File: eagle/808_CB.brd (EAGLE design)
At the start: 100 x 80 mm, 54 parts, among them IC1 4584N, IC4 TL072P, Q1 2N3904, Q2 2N3904, Q3 2N3904, Q8 2N3906

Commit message: starting board part by part
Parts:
- moved R15* 127.8 mm to (-77.5, 62.2), turned to 0 degrees
- moved C7 127.2 mm to (-31.8, 41.9)
- moved R16 109.2 mm to (-16.5, 68.6)
- moved IC4 101.8 mm to (-71.1, 31.8), turned to 0 degrees
- moved R166* 99.6 mm to (-63.5, 49.5), turned to 0 degrees
- moved PWR1 88.4 mm to (-47.0, 33.0)
- moved OUT_NORM 86.8 mm to (-62.2, 31.8), turned to 0 degrees
- moved R22 86.5 mm to (-62.2, 68.6), turned to 0 degrees
- moved C4 76.3 mm to (-55.9, 48.3)
- moved C10 70.0 mm to (-50.8, 41.9), turned to 0 degrees
- moved C9 69.0 mm to (-44.5, 41.9)
- moved R4 68.6 mm to (-54.6, 55.9), turned to 0 degrees
- moved C12 68.1 mm to (-57.1, 41.9), turned to 0 degrees
- moved C3 65.4 mm to (-45.7, 48.3), turned to 0 degrees
- moved C8 63.1 mm to (-38.1, 41.9), turned to 0 degrees
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
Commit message: part by part
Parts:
- removed 540HZ, 800HZ: 200k, pot:3RP/1610N
- removed IC4: TL072P, linear:DIL08
- removed R166*: 1K, TR808clone:0207/5V
- removed R3*: 22K, TR808clone:0207/5V
- added IC2: TL072P, linear:DIL08
- added R26: 1k, TR808clone:0207/5V
- added R27: 8k2, TR808clone:0207/5V
- added R29: 22k, TR808clone:0207/5V
- added R30: 1K, TR808clone:0207/5V
- C10: value 3.3n -> 0.47uF/50; device TR808clone:C035-025X75 -> rcl:B45181A
- C5: value 0.47uF/50 -> 2.2n; device rcl:B45181A -> TR808clone:C035-025X75
- C6: value 1uF/50 -> 2.2n; device rcl:B45181A -> TR808clone:C035-025X75
- C7: value 2.2n -> 3.3n
- C8: value 2.2n -> 10n
- C9: value 10n -> 1uF/50; device TR808clone:C035-025X75 -> rcl:B45181A
- R10, R9: value 470k -> 2k2
- R11, R12: value 100R -> 470k
- R13: value 1k -> 100R
- R14: value 33k -> 100R
- R20: value 470k -> 33k
- R21: value 8k2 -> 470k
- R22: value 22k -> 22K
- R3, R4: value 33k -> 200k; device TR808clone:0207/5V -> pot:3RP/1610N
- R7, R8: value 2k2 -> 33k
- moved R22 114.9 mm to (43.2, 22.9)
- moved R15 101.4 mm to (27.9, 35.6), turned to 180 degrees
- moved C5 97.5 mm to (24.1, 26.7), turned to 270 degrees
- moved D1 96.8 mm to (33.0, 40.6), turned to 90 degrees
- moved R11 95.2 mm to (24.1, 49.5), turned to 270 degrees
- moved D2 93.2 mm to (19.1, 40.6), turned to 90 degrees
- moved C12 92.5 mm to (29.2, 8.89)
- moved R21 86.3 mm to (17.8, 21.6), turned to 180 degrees
- moved R13 82.9 mm to (25.4, 40.6)
- moved R14 78.0 mm to (12.7, 40.6), turned to 180 degrees
- moved C3 75.0 mm to (29.2, 52.1), turned to 90 degrees
- moved R19 71.1 mm to (22.9, 34.3), turned to 270 degrees
- moved C4 70.0 mm to (14.0, 52.1), turned to 90 degrees
- moved R17 65.9 mm to (30.5, 31.8)
- moved R9 63.7 mm to (31.8, 57.1), turned to 180 degrees
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- renumbered 540HZ1 to R28, OUTPUT to JCK1, OUT_NORM to X1, Q8 to Q4, R10* to R25, R15* to R24, R6* to R23
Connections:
- net +15V: now also IC2.8, R11.2, R12.2; no longer IC4.8, R10.2, R9.2
- net -15V: now also IC2.4; no longer IC4.4
- net CY_OUT: now also R30.2; no longer R166*.2
- net GND: now also C10.-, C9.-, IC2.3, R10.1, R13.1, R14.1, R29.1, R9.1; no longer C5.-, C6.-, IC4.3, R11.1, R12.1, R22.1, R7.1, R8.1
- net LT: now also R22.2; no longer R3*.2
- net N$10: now also R9.2; no longer R3.2
- net N$11: now also R12.1; no longer R10.1
- net N$12: now also R11.1; no longer R9.1
- net N$13: now also R13.2; no longer R11.2
- net N$14: now also R14.2; no longer R12.2
- net N$15: now also D2.C; no longer D1.C
- net N$16: now also D1.C; no longer D2.C
- net N$17: now also C10.+, R20.2; no longer C5.+, R14.2
- net N$18: now also R26.2; no longer R13.2
- net N$19: now also R26.1; no longer R13.1
- net N$20: now also C9.+, R20.1; no longer C6.+, R14.1
- net N$21: now also D2.A; no longer D1.A
- net N$22: now also D1.A; no longer D2.A
- net N$23: now also C5.P$1; no longer C8.P$1
- net N$24: now also C6.P$1; no longer C7.P$1
- net N$25: now also C5.P$2, C6.P$2, C7.P$1, C8.P$1; no longer C10.P$1, C7.P$2, C8.P$2, C9.P$1
- net N$26: now also C8.P$2, IC2.2, R21.1; no longer C9.P$2, IC4.2, R20.1
- net N$27: now also C7.P$2, IC2.1, R21.2; no longer C10.P$2, IC4.1, R20.2
- net N$29: now also R27.1; no longer R21.1
- net N$30: now also R27.2; no longer R21.2
- net N$32: now also IC2.5, R29.2; no longer IC4.5, R22.2
- net N$33: now also IC2.6, IC2.7, R30.1; no longer IC4.6, IC4.7, R166*.1
- net N$4: now also R4.2; no longer 800HZ.2
- net N$5: now also R3.2; no longer 540HZ.2
- net N$517: now also R22.1; no longer R3*.1
- net N$6: now also R7.1; no longer R3.1
- net N$7: now also R3.3; no longer 540HZ.3
- net N$8: now also R4.3; no longer 800HZ.3
- net N$9: now also R10.2; no longer R4.2
- net TP7: now also R8.1; no longer R4.1

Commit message: parts on the board
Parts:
- moved R23 123.2 mm to (45.7, 54.6), turned to 270 degrees
- moved C10 121.3 mm to (47.0, 62.2), turned to 270 degrees
- moved Q4 120.3 mm to (41.9, 44.5)
- moved R24 116.9 mm to (38.1, 44.5), turned to 270 degrees
- moved R20 106.8 mm to (44.5, 67.3)
- moved R26 98.6 mm to (43.2, 49.5), turned to 180 degrees
- moved Q3 94.4 mm to (41.9, 55.9), turned to 180 degrees
- moved PWR1 92.9 mm to (44.5, 16.5), turned to 90 degrees
- moved X1 88.0 mm to (21.6, 5.08), turned to 90 degrees
- moved R25 85.4 mm to (38.1, 54.6), turned to 270 degrees
- moved D3 73.6 mm to (44.5, 39.4), turned to 180 degrees
- moved C9 66.3 mm to (41.9, 62.2), turned to 270 degrees
- moved R22 21.7 mm to (45.7, 44.5), turned to 270 degrees
- moved R29 6.84 mm to (29.2, 8.89), turned to 0 degrees
- moved R30 4.02 mm to (21.6, 12.7)
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- renumbered R28 to LEVEL, R3 to TUNE_1, R4 to TUNE_2

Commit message: routed
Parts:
- R8: device TR808clone:0207/5V -> TR808clone:0207/7
- moved R26 12.5 mm to (41.9, 37.1), turned to 0 degrees
- moved D3 10.5 mm to (36.1, 33.0), turned to 90 degrees
- moved R30 9.44 mm to (18.4, 3.81)
- moved R16 7.13 mm to (24.9, 34.8)
- moved R5 6.12 mm to (13.7, 66.8), turned to 0 degrees
- moved C12 5.99 mm to (26.0, 10.2)
- moved R13 4.33 mm to (25.1, 45.0)
- moved D2 3.94 mm to (15.2, 39.6)
- moved R29 3.59 mm to (31.8, 6.35)
- moved R15 3.59 mm to (30.5, 38.1), turned to 90 degrees
- moved C11 3.34 mm to (21.1, 17.0), turned to 90 degrees
- moved R19 3.31 mm to (19.6, 34.5)
- moved R23 3.09 mm to (48.8, 54.1)
- moved C5 2.97 mm to (26.9, 25.7), turned to 180 degrees
- moved R18 2.84 mm to (14.0, 31.8), turned to 0 degrees
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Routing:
- net GND: track 0.00 -> 268.4 mm
- net +5V: track 0.00 -> 101.6 mm
- net +15V: track 0.00 -> 77.6 mm
- net N$7: track 0.00 -> 52.6 mm, vias 0 -> 2
- net N$17: track 0.00 -> 49.8 mm
- net N$33: track 0.00 -> 34.9 mm
- net -15V: track 0.00 -> 33.7 mm
- net N$5: track 0.00 -> 31.1 mm
- net N$31: track 0.00 -> 26.9 mm
- net N$27: track 0.00 -> 26.4 mm
- net TRIG*: track 0.00 -> 23.9 mm
- net N$25: track 0.00 -> 21.2 mm
- net N$8: track 0.00 -> 17.1 mm
- net LT: track 0.00 -> 15.9 mm
- net N$32: track 0.00 -> 14.9 mm
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
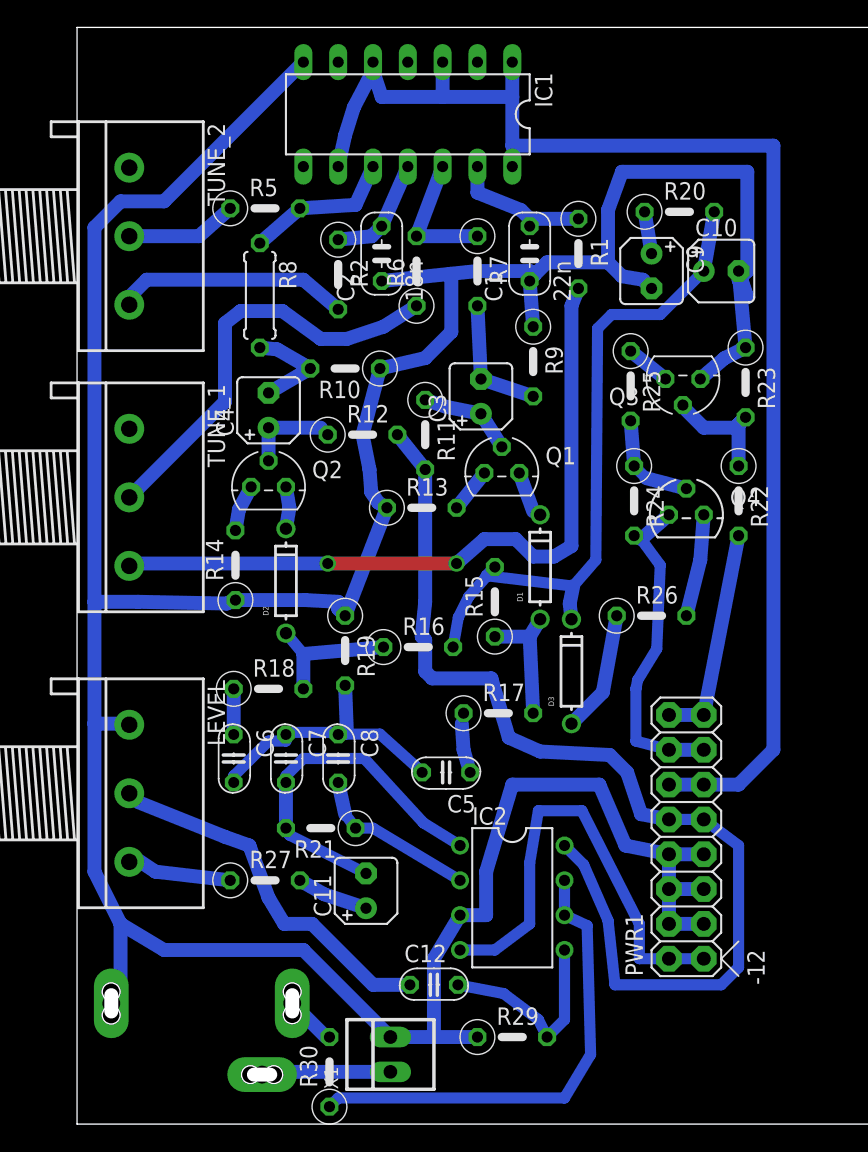
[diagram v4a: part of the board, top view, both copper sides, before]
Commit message: thicker traces
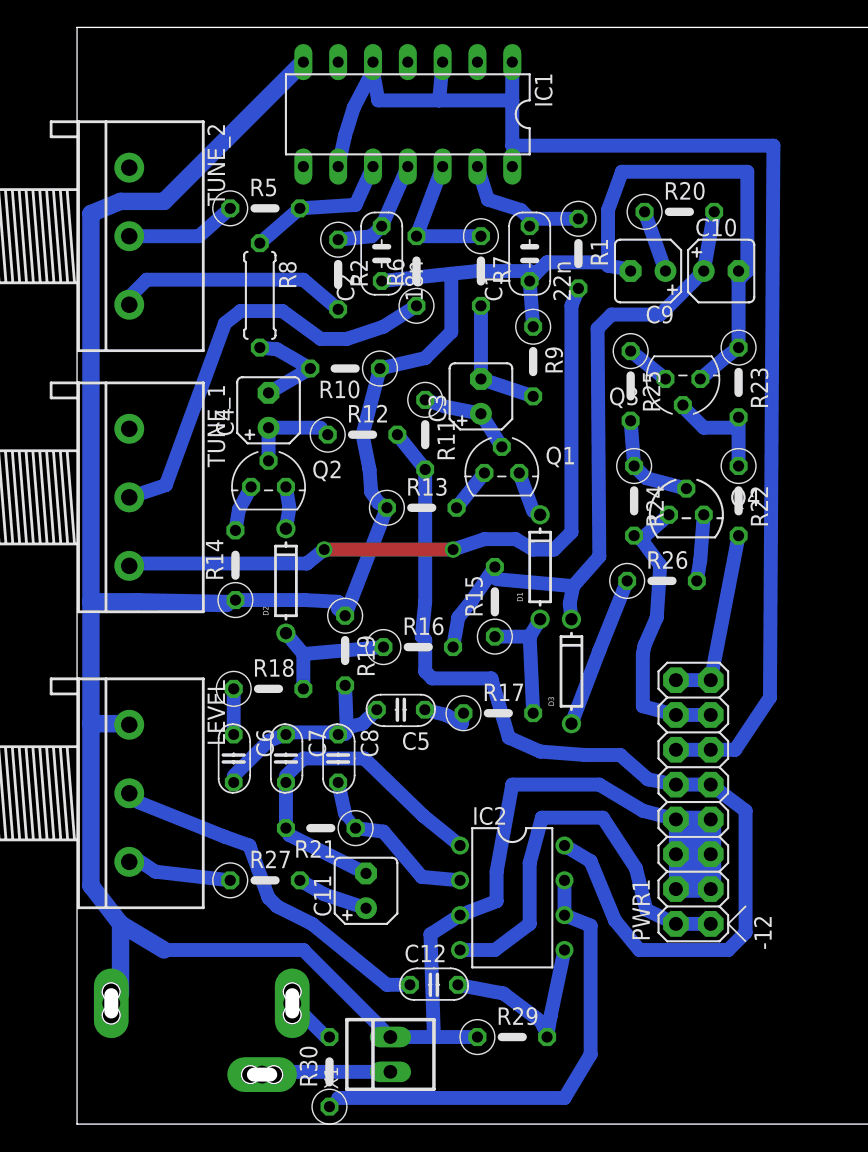
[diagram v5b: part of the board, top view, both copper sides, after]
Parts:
- moved C5 5.64 mm to (23.6, 30.2)
- moved R26 2.65 mm to (42.7, 39.6)
- moved PWR1 2.59 mm to (45.0, 21.0)
- moved R23 0.51 mm to (48.3, 54.1)
- moved C9 0.25 mm to (41.7, 62.2), turned to 180 degrees
- moved R7 0.25 mm to (29.5, 62.2)
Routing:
- net GND: track 268.4 -> 263.2 mm
- net +15V: track 77.6 -> 73.3 mm
- net N$25: track 21.2 -> 17.2 mm
- net -15V: track 33.7 -> 30.5 mm
- net +5V: track 101.6 -> 98.7 mm
- net TRIG*: track 23.9 -> 21.2 mm
- net N$18: track 7.50 -> 4.86 mm
- net LT: track 15.9 -> 13.3 mm
- net N$19: track 8.91 -> 11.2 mm
- net N$20: track 3.09 -> 4.58 mm
- net N$7: track 52.6 -> 51.4 mm
- net N$31: track 26.9 -> 26.1 mm
- net N$23: track 4.40 -> 3.68 mm
- net N$17: track 49.8 -> 49.1 mm
- net N$26: track 12.3 -> 12.8 mm

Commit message: trigger and accent pads
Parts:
- added ACCENT, TRIGGER: LSP11, solpad:LSP11
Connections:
- net LT: now also TRIGGER.MP
- net TRIG*: now also ACCENT.MP
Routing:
- net LT: track 13.3 -> 18.3 mm
- net TRIG*: track 21.2 -> 23.5 mm
- net N$19: track 11.2 -> 11.9 mm
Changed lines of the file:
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@@
 <element name="R10" library="TR808clone" package="0207/5V" value="2k2" x="19.558" y="55.118" rot="R180"/>
 <element name="R11" library="TR808clone" package="0207/5V" value="470k" x="25.4" y="50.292" rot="R270"/>
+<element name="TRIGGER" library="solpad" package="LSP11" value="LSP11" x="45.212" y="36.322"/>
+<element name="ACCENT" library="solpad" package="LSP11" value="LSP11" x="39.116" y="29.972"/>
 </elements>
 <signals>
@@
 <wire x1="41.275" y1="30.48" x2="41.275" y2="34.29" width="1.016" layer="16"/>
 <wire x1="43.688" y1="29.845" x2="41.275" y2="30.48" width="1.016" layer="16"/>
+<contactref element="ACCENT" pad="MP"/>
+<wire x1="41.275" y1="30.48" x2="39.624" y2="30.48" width="1.016" layer="16"/>
+<wire x1="39.624" y1="30.48" x2="39.116" y2="29.972" width="1.016" layer="16"/>
 </signal>
 <signal name="+5V">
@@
 <contactref element="PWR1" pad="16"/>
 <contactref element="R22" pad="2"/>
-<wire x1="46.228" y1="32.385" x2="48.26" y2="42.926" width="1.016" layer="16"/>
+<wire x1="46.228" y1="32.385" x2="48.26" y2="35.052" width="1.016" layer="16"/>
+<wire x1="48.26" y1="35.052" x2="48.26" y2="42.926" width="1.016" layer="16"/>
 <wire x1="46.228" y1="32.385" x2="43.688" y2="32.385" width="1.016" layer="16"/>
+<contactref element="TRIGGER" pad="MP"/>
+<wire x1="43.688" y1="32.385" x2="43.688" y2="34.798" width="1.016" layer="16"/>
+<wire x1="43.688" y1="34.798" x2="45.212" y2="36.322" width="1.016" layer="16"/>
 </signal>
 <signal name="+15V">
@@
 <wire x1="33.274" y1="41.91" x2="32.004" y2="42.672" width="1.016" layer="16"/>
 <wire x1="32.004" y1="42.672" x2="29.718" y2="42.672" width="1.016" layer="16"/>
-<wire x1="29.718" y1="42.672" x2="27.432" y2="41.91" width="1.016" layer="16"/>
-<via x="27.432" y="41.91" extent="1-16" drill="0.8" shape="square"/>
-<wire x1="27.432" y1="41.91" x2="18.034" y2="41.91" width="1.016" layer="1"/>
+<wire x1="29.718" y1="42.672" x2="27.94" y2="41.91" width="1.016" layer="16"/>
+<via x="27.94" y="41.91" extent="1-16" drill="0.8" shape="square"/>
+<wire x1="27.94" y1="41.91" x2="18.034" y2="41.91" width="1.016" layer="1"/>
 <via x="18.034" y="41.91" extent="1-16" drill="0.8" shape="square"/>
 <wire x1="18.034" y1="41.91" x2="16.764" y2="40.894" width="1.016" layer="16"/>
@@
 <contactref element="D3" pad="A"/>
 <contactref element="R26" pad="1"/>
-<wire x1="40.132" y1="39.624" x2="38.1" y2="34.544" width="1.016" layer="16"/>
-<wire x1="38.1" y1="34.544" x2="36.068" y2="29.21" width="1.016" layer="16"/>
+<wire x1="40.132" y1="39.624" x2="38.608" y2="35.306" width="1.016" layer="16"/>
+<wire x1="38.608" y1="35.306" x2="36.068" y2="33.274" width="1.016" layer="16"/>
+<wire x1="36.068" y1="33.274" x2="36.068" y2="29.21" width="1.016" layer="16"/>
 </signal>
 <signal name="N$20">

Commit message: tweaks and cleanups
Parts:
- moved R29 0.51 mm to (31.8, 6.86)
- moved X1 0.51 mm to (22.9, 5.59)
- moved R30 0.51 mm to (18.4, 4.32)
- moved C12 0.36 mm to (25.8, 9.91)
- moved R24 0.36 mm to (40.4, 45.7)
- moved D1 0.25 mm to (33.5, 40.6)
- moved R6 0.25 mm to (24.8, 62.0)
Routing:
- net N$25: track 17.2 -> 15.3 mm
- net GND: track 263.2 -> 262.4 mm
- net N$23: track 3.68 -> 2.84 mm
- net N$32: track 14.5 -> 13.8 mm

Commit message: tweaks and cleanups
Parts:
- moved R20 6.53 mm to (42.4, 60.2), turned to 180 degrees
- moved C10 6.49 mm to (41.4, 65.5), turned to 90 degrees
- moved TRIGGER 6.25 mm to (48.0, 41.9)
- moved C9 5.64 mm to (46.2, 65.5), turned to 90 degrees
- moved R22 4.44 mm to (46.0, 49.3), turned to 0 degrees
- moved D3 3.05 mm to (36.1, 36.1)
- moved ACCENT 2.90 mm to (36.3, 29.2)
- moved R21 1.02 mm to (18.8, 21.6)
- moved R30 0.80 mm to (18.2, 5.08)
- moved R23 0.76 mm to (48.3, 54.9)
- moved R15 0.25 mm to (30.5, 37.8)
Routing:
- net GND: track 262.4 -> 250.9 mm
- net N$17: track 49.6 -> 39.3 mm
- net TRIG*: track 23.9 -> 27.0 mm
- net N$19: track 11.9 -> 8.89 mm
- net LT: track 18.3 -> 20.0 mm
- net +5V: track 98.7 -> 97.2 mm
- net N$517: track 8.93 -> 7.60 mm
- net CY_OUT: track 4.05 -> 2.76 mm
- net N$29: track 8.34 -> 7.54 mm
- net N$8: track 17.1 -> 16.3 mm
- net N$26: track 12.8 -> 12.2 mm
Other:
- board size 100 x 80 mm -> 100.8 x 81.3 mm
